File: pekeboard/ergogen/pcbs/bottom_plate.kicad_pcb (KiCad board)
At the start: 2 copper layers, 150.9 x 124.7 mm, 0 parts

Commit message: pekepad folder fix
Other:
- outline, holes or cut-outs redrawn

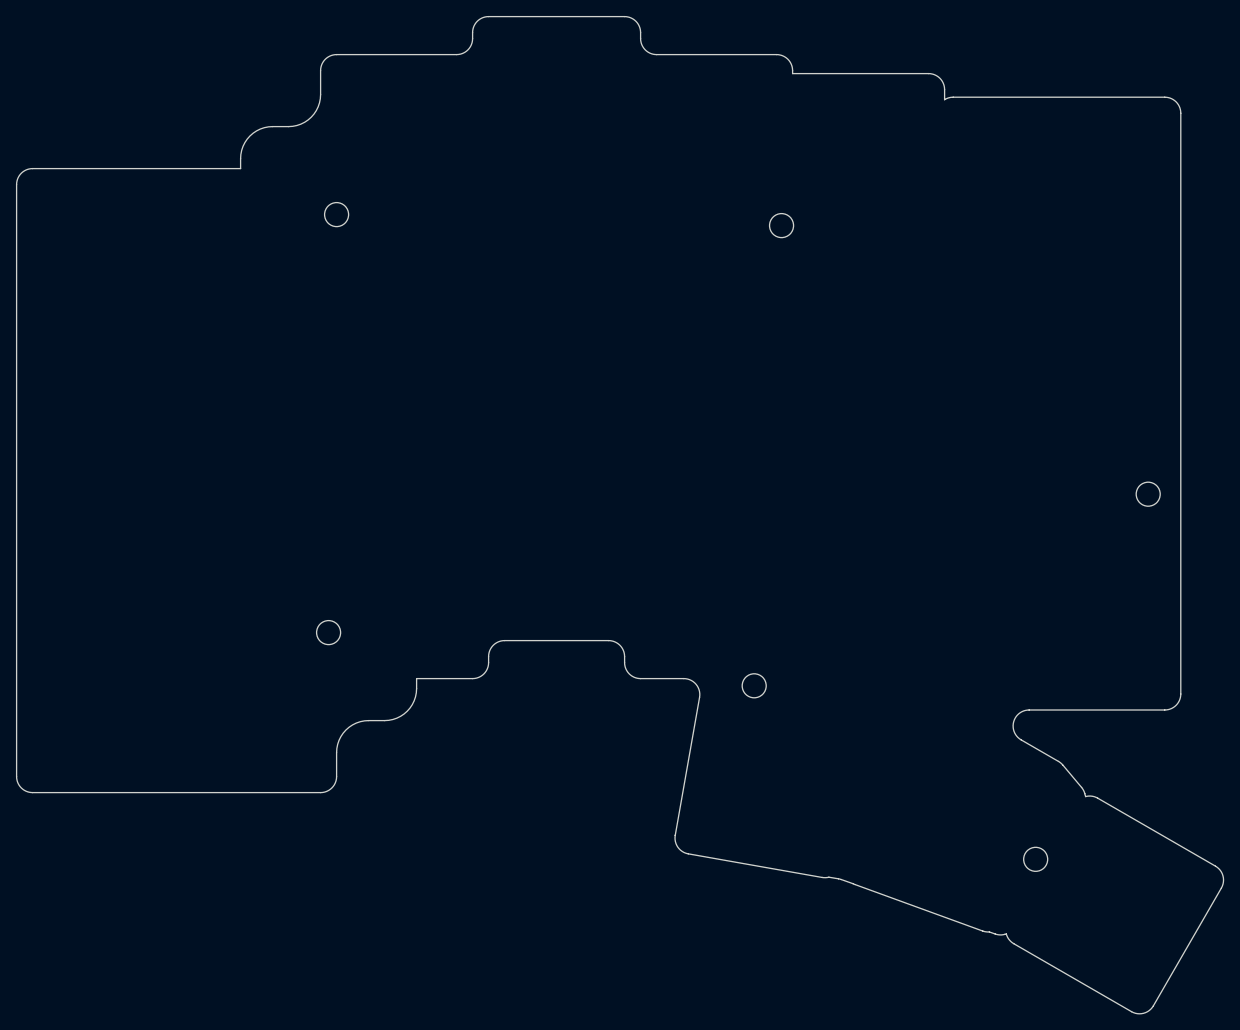
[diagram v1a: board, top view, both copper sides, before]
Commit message: Less spread for thumb cluster
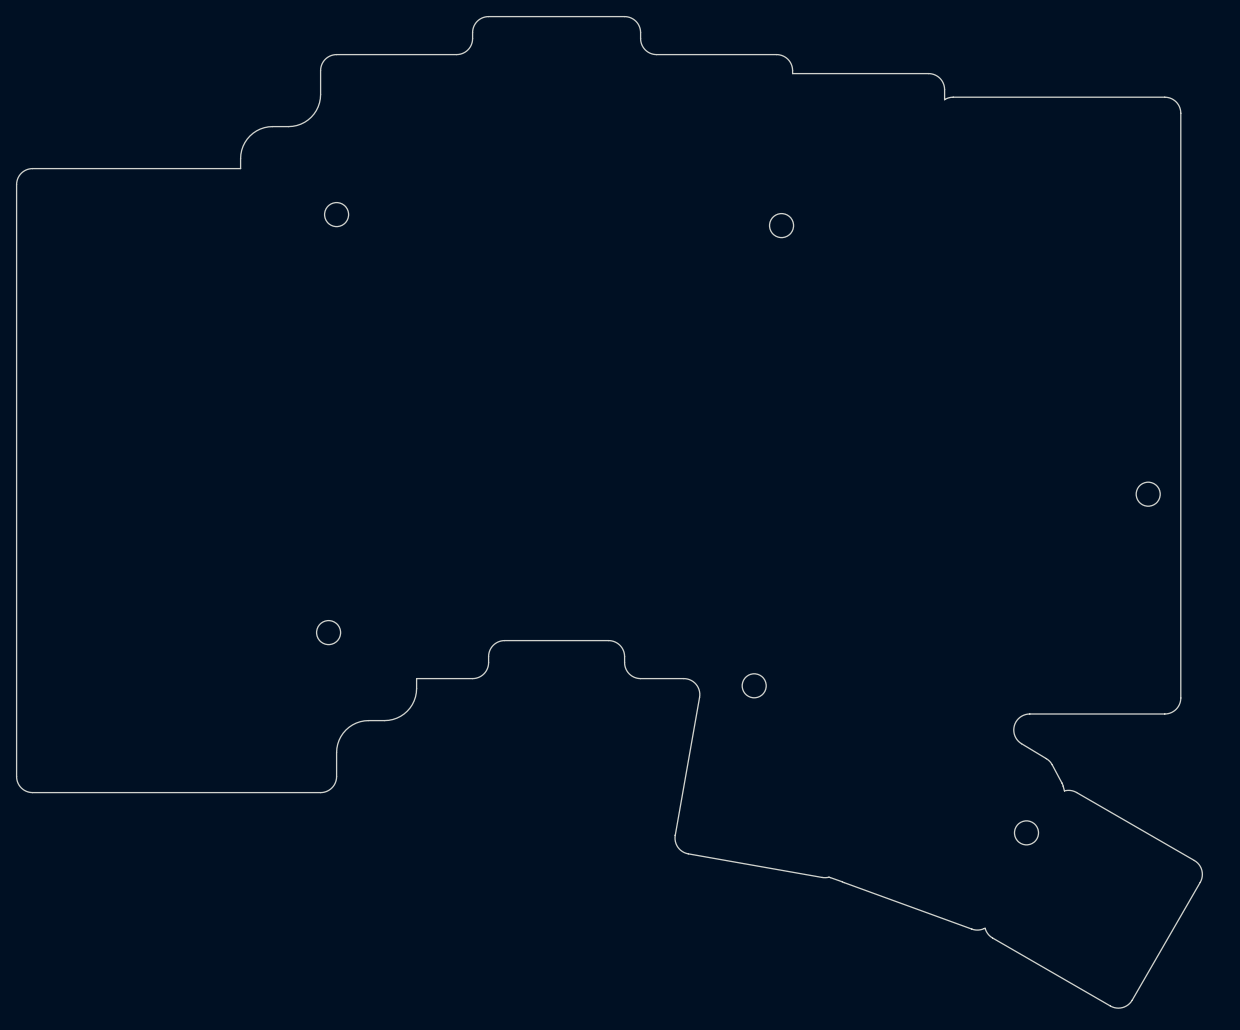
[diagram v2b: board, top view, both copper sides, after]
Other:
- board size 150.9 x 124.7 mm -> 148.2 x 123.9 mm
